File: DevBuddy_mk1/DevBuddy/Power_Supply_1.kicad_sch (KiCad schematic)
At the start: 1 part, among them U5 TPS54331DDAR

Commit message: Changes is hardware - Power
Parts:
- added C10, C11, C18, C19, C20, C9: 4u7, Capacitor_SMD:C_1210_3225Metric, symbol Device:C_Small
- added C12: 6p8, Capacitor_SMD:C_0402_1005Metric, symbol Device:C_Small
- added C13: 3n3, Capacitor_SMD:C_0402_1005Metric, symbol Device:C_Small
- added C14, C21: 8n2, Capacitor_SMD:C_0402_1005Metric, symbol Device:C_Small
- added C15, C22: 100n, Capacitor_SMD:C_0805_2012Metric, symbol Device:C_Small
- added C16, C17: 220u, Capacitor_SMD:CP_Elec_6.3x5.4, symbol Device:C_Polarized_Small
- added C23: 1n, Capacitor_SMD:C_0402_1005Metric, symbol Device:C_Small
- added C24: 10p, Capacitor_SMD:C_0402_1005Metric, symbol Device:C_Small
- added C25, C26, C27: 10u, Capacitor_SMD:C_1210_3225Metric, symbol Device:C_Small
- added C28, C40: 470n, Capacitor_SMD:C_0402_1005Metric, symbol Device:C_Small
- added C29, C39: 2n2, Capacitor_SMD:C_0402_1005Metric, symbol Device:C_Small
- added C30, C31, C37, C38, C41, C42, C46, C47, C48, C49: 22u, Capacitor_SMD:C_0805_2012Metric, symbol Device:C_Small
- added C32, C33, C43, C44: 47u, Capacitor_SMD:C_0805_2012Metric, symbol Device:C_Small
- added C34, C35, C36: 10u, Capacitor_SMD:C_0805_2012Metric, symbol Device:C_Small
- added D1: 550mV 5A, Diode_SMD:D_SMC, symbol Device:D_Small
- added D2: 550mV 2A, Diode_SMD:D_SMC, symbol Device:D_Small
- added FB1, FB2: 0H 1mOhm, symbol Device:FerriteBead_Small
- added L2: 33u, Inductor_SMD:L_Coilcraft_MSS1210-XXX, symbol Device:L_Small
- added L3, L5: 4u7, Inductor_SMD:L_Coilcraft_XAL6060-XXX, symbol Device:L_Small
- added L4: 15u, Inductor_SMD:L_Bourns_SRR1260, symbol Device:L
- added R10: 42k2, Resistor_SMD:R_0402_1005Metric, symbol Device:R_Small
- added R11, R5: 18k7, Resistor_SMD:R_0402_1005Metric, symbol Device:R_Small
- added R12: 28k7, Resistor_SMD:R_0402_1005Metric, symbol Device:R_Small
- added R13, R8: 10k2, Resistor_SMD:R_01005_0402Metric, symbol Device:R_Small
- added R14: 732R, Resistor_SMD:R_01005_0402Metric, symbol Device:R_Small
- added R15, R18: 10k, Resistor_SMD:R_0402_1005Metric, symbol Device:R_Small
- added R16, R19: 15k4, Resistor_SMD:R_0402_1005Metric, symbol Device:R_Small
- added R17, R20: 4k87, Resistor_SMD:R_0402_1005Metric, symbol Device:R_Small
- added R6, R7: 169k, Resistor_SMD:R_0402_1005Metric, symbol Device:R_Small
- added R9: 3k24, Resistor_SMD:R_01005_0402Metric, symbol Device:R_Small
- added U6: TPS54331DDAR, TPS54331DDAR:CONV_TPS54331DDAR, symbol TPS54331DDAR:TPS54331DDAR
- added U7, U8: TPS62913, Package_DFN_QFN:Texas_RPU0010A_VQFN-HR-10_2x2mm_P0.5mm, symbol Regulator_Switching:TPS62913
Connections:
- net at U5.1 (BOOT): now also C15.1
- net VCC: now reaches U5.2 (VIN)
- net VCC: now also C10.1, C11.1, C18.1, C19.1, C20.1, C9.1, R6.1, R7.1, U6.2 (VIN)
- net at U5.3 (EN): now also R5.1, R7.2
- net at U5.4 (SS): now also C14.1
- net at U5.5 (VSENSE): now also R8.1, R9.2
- net at U5.6 (COMP): now also C12.1, R10.1
- net GND: now reaches U5.7 (GND)
- net GND: now also U5.9 (POWERPAD), C10.2, C11.2, C12.2, C13.2, C14.2, C16.2, C17.2, C18.2, C19.2, C20.2, C21.2, C23.2, C24.2, C25.2, C26.2, C27.2, C28.2, C29.2, C30.2, C31.2, C32.2, C33.2, C34.2, C35.2, C36.2, C37.2, C38.2, C39.2, C40.2, C41.2, C42.2, C43.2, C44.2, C46.2, C47.2, C48.2, C49.2, C9.2, D1.2 (A), D2.2 (A), R11.2, R14.1, R17.2, R20.2, R5.2, R9.1, U6.7 (GND), U6.9 (POWERPAD), U7.10 (S-CONF), U7.4 (PGND), U7.7 (PSNS), U8.4 (PGND), U8.7 (PSNS)
- net at U5.8 (PH): now also C15.2, D1.1 (K), L2.1
- new net: C41.1, C42.1, C46.1, C47.1, C48.1, C49.1, FB2.1, L5.2, R18.1, U8.3 (VO)
- new net: C13.1, R10.2
- new net: R18.2, U8.5 (PG)
- new net: L3.1, U7.2 (SW)
- new net: C32.1, C33.1, FB1.1, L3.2, R15.1, U7.3 (VO)
- new net: L5.1, U8.2 (SW)
- new net: C40.1, U8.8 (NR/SS)
- new net: R11.1, R6.2, U6.3 (EN)
- new net: R13.1, R14.2, U6.5 (VSENSE)
- new net: C22.1, U6.1 (BOOT)
- new net: C21.1, U6.4 (SS)
- new net: C24.1, R12.1, U6.6 (COMP)
- new net: C22.2, D2.1 (K), L4.1, U6.8 (PH)
- new net: R15.2, U7.5 (PG)
- new net: C28.1, U7.8 (NR/SS)
- new net: C23.1, R12.2
- new net +12VDC: C25.1, C26.1, C27.1, C29.1, C30.1, C31.1, C37.1, C38.1, C39.1, L4.2, R13.2, U7.1 (EN/SYNC), U7.6 (VIN), U8.1 (EN/SYNC), U8.10 (S-CONF), U8.6 (VIN)
- new net +3V3: C16.1, C17.1, L2.2, R8.2
- new net +3V3_C: C34.1, C35.1, C36.1, FB1.2, R16.1
- new net +5V_C: C43.1, C44.1, FB2.2, R19.1
- new net buck_fb: R16.2, R17.1, R19.2, R20.1, U7.9 (FB), U8.9 (FB)
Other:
- note added: "12V Supply for Low Voltage Clean Channels @2A / 24W"
- note added: "3V3 Logic Power supply @1A / 3.3W (could go up to 6.6W)"
- note added: "3V3 clean Channel Power supply @3A / 9.9W"
- note added: "5V clean Channel Power supply @3A / 15W"
- moved on the sheet: U5

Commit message: Added mux control, fixed adc tlm control, fixed app, added power in PCB
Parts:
- added C45, C50, C53, C54, C64, C67, C68, C70, C72, C75: 22u, Capacitor_SMD:C_0805_2012Metric, symbol Device:C_Small
- added C51, C52, C55: 4u7, Capacitor_SMD:C_1210_3225Metric, symbol Device:C_Small
- added C56, C57: 2n2, Capacitor_SMD:C_0402_1005Metric, symbol Device:C_Small
- added C58, C59: 470n, Capacitor_SMD:C_0402_1005Metric, symbol Device:C_Small
- added C60: 8n2, Capacitor_SMD:C_0402_1005Metric, symbol Device:C_Small
- added C61: 100n, Capacitor_SMD:C_0805_2012Metric, symbol Device:C_Small
- added C62: 1n, Capacitor_SMD:C_0402_1005Metric, symbol Device:C_Small
- added C63, C66, C78, C79: 47u, Capacitor_SMD:C_0805_2012Metric, symbol Device:C_Small
- added C65: 10p, Capacitor_SMD:C_0402_1005Metric, symbol Device:C_Small
- added C69, C71, C73: 10u, Capacitor_SMD:C_0805_2012Metric, symbol Device:C_Small
- added C74, C76, C77: 10u, Capacitor_SMD:C_1210_3225Metric, symbol Device:C_Small
- added D3: 550mV 2A, Diode_SMD:D_SMC, symbol Device:D_Small
- added FB3, FB4: 0H 1mOhm, symbol Device:FerriteBead_Small
- added L6, L7: 4u7, Inductor_SMD:L_Coilcraft_XAL6060-XXX, symbol Device:L_Small
- added L8: 15u, Inductor_SMD:L_Bourns_SRR1260, symbol Device:L
- added R21: 169k, Resistor_SMD:R_0402_1005Metric, symbol Device:R_Small
- added R22: 18k7, Resistor_SMD:R_0402_1005Metric, symbol Device:R_Small
- added R23, R24: 10k, Resistor_SMD:R_0402_1005Metric, symbol Device:R_Small
- added R25: 28k7, Resistor_SMD:R_0402_1005Metric, symbol Device:R_Small
- added R26: 10k2, Resistor_SMD:R_01005_0402Metric, symbol Device:R_Small
- added R27: 732R, Resistor_SMD:R_01005_0402Metric, symbol Device:R_Small
- added R28, R30: 15k4, Resistor_SMD:R_0402_1005Metric, symbol Device:R_Small
- added R29, R31: 4k87, Resistor_SMD:R_0402_1005Metric, symbol Device:R_Small
- added U10, U9: TPS62913, Package_DFN_QFN:Texas_RPU0010A_VQFN-HR-10_2x2mm_P0.5mm, symbol Regulator_Switching:TPS62913
- added U11: TPS54331DDAR, TPS54331DDAR:CONV_TPS54331DDAR, symbol TPS54331DDAR:TPS54331DDAR
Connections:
- net GND: now also C45.2, C50.2, C51.2, C52.2, C53.2, C54.2, C55.2, C56.2, C57.2, C58.2, C59.2, C60.2, C62.2, C63.2, C64.2, C65.2, C66.2, C67.2, C68.2, C69.2, C70.2, C71.2, C72.2, C73.2, C74.2, C75.2, C76.2, C77.2, C78.2, C79.2, D3.2 (A), R22.2, R27.1, R29.2, R31.2, U10.4 (PGND), U10.7 (PSNS), U11.7 (GND), U11.9 (POWERPAD), U9.10 (S-CONF), U9.4 (PGND), U9.7 (PSNS)
- net VCC: now also C51.1, C52.1, C55.1, R21.1, U11.2 (VIN)
- net buck_fb: now also R28.2, R29.1, R30.2, R31.1, U10.9 (FB), U9.9 (FB)
- net +12VDC renamed +12VDC_C
- new net: C61.1, U11.1 (BOOT)
- new net: R21.2, R22.1, U11.3 (EN)
- new net: C60.1, U11.4 (SS)
- new net: R26.1, R27.2, U11.5 (VSENSE)
- new net: C65.1, R25.1, U11.6 (COMP)
- new net: C61.2, D3.1 (K), L8.1, U11.8 (PH)
- new net: C64.1, C67.1, C68.1, C70.1, C72.1, C75.1, FB4.1, L7.2, R24.1, U10.3 (VO)
- new net: L7.1, U10.2 (SW)
- new net: L6.1, U9.2 (SW)
- new net: C63.1, C66.1, FB3.1, L6.2, R23.1, U9.3 (VO)
- new net: R24.2, U10.5 (PG)
- new net: C59.1, U10.8 (NR/SS)
- new net: C62.1, R25.2
- new net: R23.2, U9.5 (PG)
- new net: C58.1, U9.8 (NR/SS)
- new net +12VDC_D: C45.1, C50.1, C53.1, C54.1, C56.1, C57.1, C74.1, C76.1, C77.1, L8.2, R26.2, U10.1 (EN/SYNC), U10.10 (S-CONF), U10.6 (VIN), U9.1 (EN/SYNC), U9.6 (VIN)
- new net +3V3_D: C69.1, C71.1, C73.1, FB3.2, R28.1
- new net +5V_D: C78.1, C79.1, FB4.2, R30.1
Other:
- note added: "12V Supply for Low Voltage Clean Channels @2A / 24W CHANNEL C"
- note added: "12V Supply for Low Voltage Clean Channels @2A / 24W CHANNEL D"
- note added: "3V3 Logic Power supply @1A / 3.3W (could go up to 6.6W) CHANNEL A"
- note added: "3V3 clean Channel Power supply @3A / 9.9W CHANNEL C"
- note added: "3V3 clean Channel Power supply @3A / 9.9W CHANNEL D"
- note added: "5V clean Channel Power supply @3A / 15W CHANNEL C"
- note added: "5V clean Channel Power supply @3A / 15W CHANNEL D"
- note removed: "12V Supply for Low Voltage Clean Channels @2A / 24W"
- note removed: "3V3 Logic Power supply @1A / 3.3W (could go up to 6.6W)"
- note removed: "3V3 clean Channel Power supply @3A / 9.9W"
- note removed: "5V clean Channel Power supply @3A / 15W"

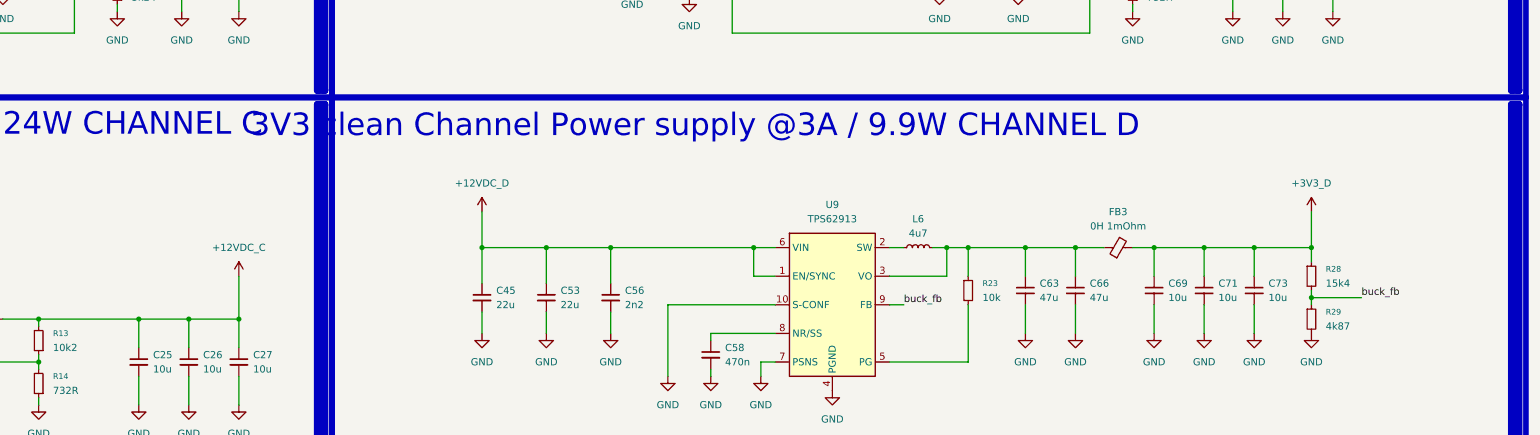
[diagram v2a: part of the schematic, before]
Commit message: Changes in Variable buck - Hardware
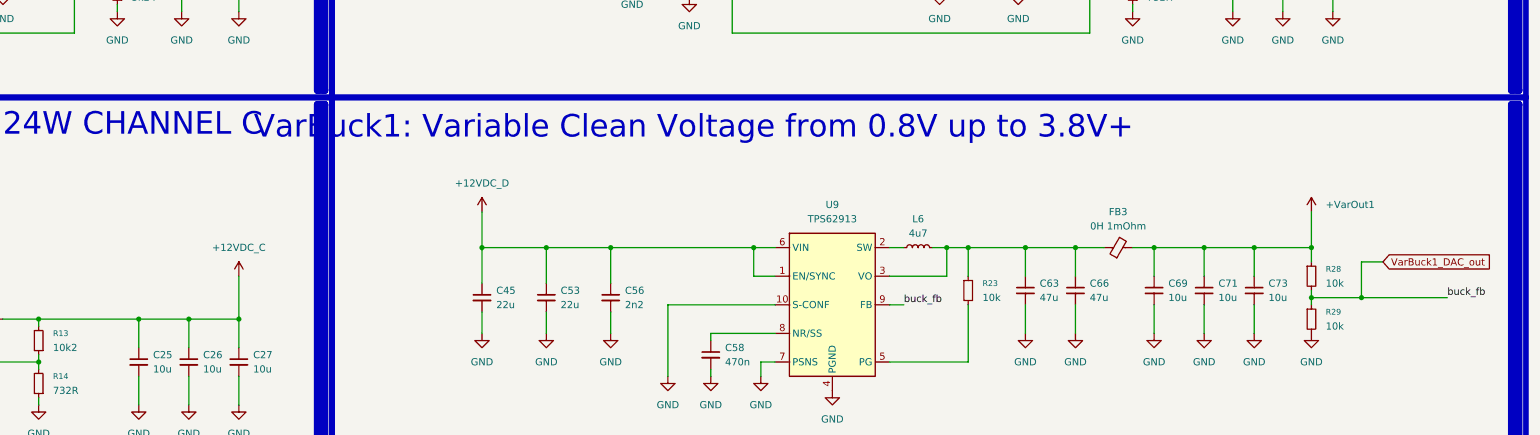
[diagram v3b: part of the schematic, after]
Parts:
- R28: value 15k4 -> 10k
- R29: value 4k87 -> 10k
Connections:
- net +3V3_D renamed +VarOut1
- net buck_fb renamed VarBuck1_DAC_out
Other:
- note added: "VarBuck1: Variable Clean Voltage from 0.8V up to 3.8V+"
- note removed: "3V3 clean Channel Power supply @3A / 9.9W CHANNEL D"
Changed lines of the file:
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@@
 		)
 	)
-	(text "3V3 clean Channel Power supply @3A / 9.9W CHANNEL D\n"
+	(text "VarBuck1: Variable Clean Voltage from 0.8V up to 3.8V+"
 		(exclude_from_sim no)
-		(at 258.826 88.9 0)
+		(at 258.572 89.154 0)
 		(effects
 			(font
@@
 	)
 	(junction
+		(at 377.19 119.38)
+		(diameter 0)
+		(color 0 0 0 0)
+	)
+	(junction
 		(at 44.45 180.34)
 		(diameter 0)
@@
 	(wire
 		(pts
+			(xy 381 113.03) (xy 377.19 113.03)
+		)
+		(stroke
+			(width 0)
+			(type default)
+		)
+	)
+	(wire
+		(pts
 			(xy 378.46 187.96) (xy 378.46 189.23)
 		)
@@
 	(wire
 		(pts
+			(xy 377.19 119.38) (xy 392.43 119.38)
+		)
+		(stroke
+			(width 0)
+			(type default)
+		)
+	)
+	(wire
+		(pts
 			(xy 44.45 250.19) (xy 44.45 256.54)
 		)
@@
 	(wire
 		(pts
+			(xy 377.19 113.03) (xy 377.19 119.38)
+		)
+		(stroke
+			(width 0)
+			(type default)
+		)
+	)
+	(wire
+		(pts
 			(xy 72.39 113.03) (xy 60.96 113.03)
 		)
@@
 	)
 	(label "buck_fb"
-		(at 377.19 119.38 0)
+		(at 392.43 119.38 0)
 		(effects
 			(font
@@
 		)
 	)
+	(global_label "VarBuck1_DAC_out"
+		(shape input)
+		(at 381 113.03 0)
+		(fields_autoplaced yes)
+		(effects
+			(font
+				(size 1.27 1.27)
+			)
+			(justify left)
+		)
+		(property "Intersheetrefs" "${INTERSHEET_REFS}"
+			(at 401.3417 113.03 0)
+			(effects
+				(font
+					(size 1.27 1.27)
+				)
+				(justify left)
+				(hide yes)
+			)
+		)
+	)
 	(symbol
 		(lib_id "power:GND")
@@
 			)
 		)
-		(property "Value" "4k87"
+		(property "Value" "10k"
 			(at 370.84 124.4599 0)
 			(effects
@@
 			)
 		)
-		(property "Value" "15k4"
+		(property "Value" "10k"
 			(at 370.84 116.8399 0)
 			(effects
@@
 			)
 		)
-		(property "Value" "+3V3_D"
-			(at 368.3 99.06 0)
+		(property "Value" "+VarOut1"
+			(at 370.84 102.8699 0)
 			(effects
 				(font
 					(size 1.27 1.27)
 				)
+				(justify left)
 			)
 		)

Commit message: Added variable voltage channels/ PCB
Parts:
- removed C45, C53: 22u, Capacitor_SMD:C_0805_2012Metric, symbol Device:C_Small
- removed C56: 2n2, Capacitor_SMD:C_0402_1005Metric, symbol Device:C_Small
- removed C58: 470n, Capacitor_SMD:C_0402_1005Metric, symbol Device:C_Small
- removed C63, C66: 47u, Capacitor_SMD:C_0805_2012Metric, symbol Device:C_Small
- removed C69, C71, C73: 10u, Capacitor_SMD:C_0805_2012Metric, symbol Device:C_Small
- removed FB3: 0H 1mOhm, symbol Device:FerriteBead_Small
- removed L6: 4u7, Inductor_SMD:L_Coilcraft_XAL6060-XXX, symbol Device:L_Small
- removed R23, R28, R29: 10k, Resistor_SMD:R_0402_1005Metric, symbol Device:R_Small
- removed U9: TPS62913, Package_DFN_QFN:Texas_RPU0010A_VQFN-HR-10_2x2mm_P0.5mm, symbol Regulator_Switching:TPS62913
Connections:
- net VarBuck1_DAC_out renamed buck_fb
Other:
- note removed: "VarBuck1: Variable Clean Voltage from 0.8V up to 3.8V+"

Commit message: Heavy additions to schematic
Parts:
- added R77, R78, R79, R80, R81: 20mOhm, Resistor_SMD:R_1210_3225Metric, symbol Device:R
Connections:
- net +12VDC_C: now also R77.1; no longer C25.1, C26.1, C27.1, L4.2, R13.2
- net +12VDC_D: now also R80.1; no longer C74.1, C76.1, C77.1, L8.2, R26.2
- net +3V3_C: now also R78.1; no longer C34.1, C35.1, C36.1, FB1.2, R16.1
- net +5V_C: now also R79.1; no longer C43.1, C44.1, FB2.2, R19.1
- net +5V_D: now also R81.1; no longer C78.1, C79.1, FB4.2, R30.1
- new net 12V_C_CurSense_Hi: C25.1, C26.1, C27.1, L4.2, R13.2, R77.2
- new net 12V_D_CurSense_Hi: C74.1, C76.1, C77.1, L8.2, R26.2, R80.2
- new net 3V3_C_CurSense_Hi: C34.1, C35.1, C36.1, FB1.2, R16.1, R78.2
- new net 5V_C_CurSense_Hi: C43.1, C44.1, FB2.2, R19.1, R79.2
- new net 5V_D_CurSense_Hi: C78.1, C79.1, FB4.2, R30.1, R81.2

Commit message: PCB, starting the board
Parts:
- FB1: footprint (none) -> Fuse:Fuse_1206_3216Metric; Field5 (none) -> C710518
- FB2, FB4: footprint (none) -> Fuse:Fuse_1206_3216Metric
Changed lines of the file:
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@@
 			)
 		)
-		(property "Footprint" ""
+		(property "Footprint" "Fuse:Fuse_1206_3216Metric"
 			(at 134.62 182.118 90)
 			(effects
@@
 			)
 		)
+		(property "Field5" "C710518"
+			(at 134.62 180.34 90)
+			(effects
+				(font
+					(size 1.27 1.27)
+				)
+				(hide yes)
+			)
+		)
 		(pin "1"
 		)
@@
 			)
 		)
-		(property "Footprint" ""
+		(property "Footprint" "Fuse:Fuse_1206_3216Metric"
 			(at 351.79 182.118 90)
 			(effects
@@
 			)
 		)
-		(property "Footprint" ""
+		(property "Footprint" "Fuse:Fuse_1206_3216Metric"
 			(at 171.45 251.968 90)
 			(effects

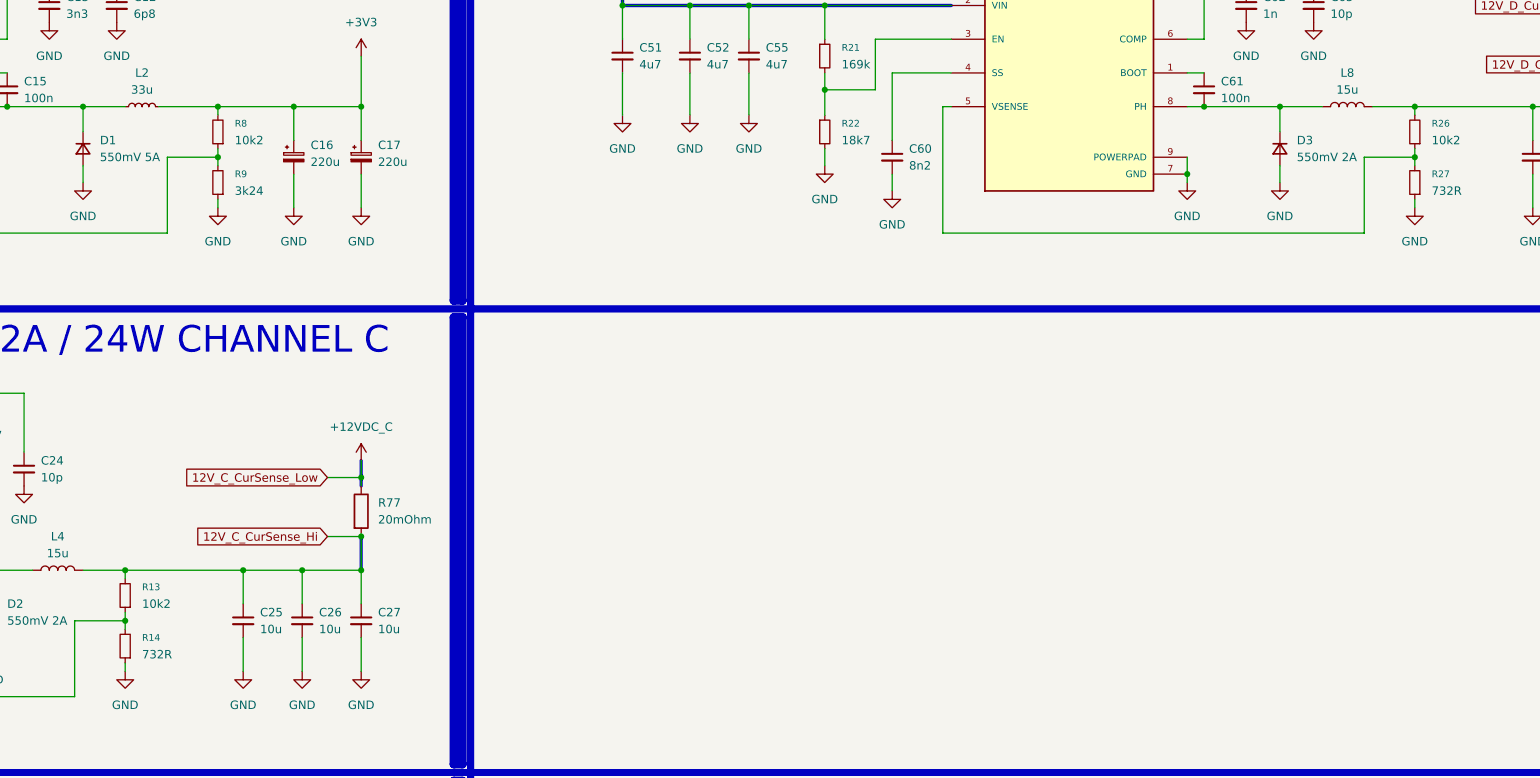
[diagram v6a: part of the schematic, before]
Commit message: PCB, initial routing of submods
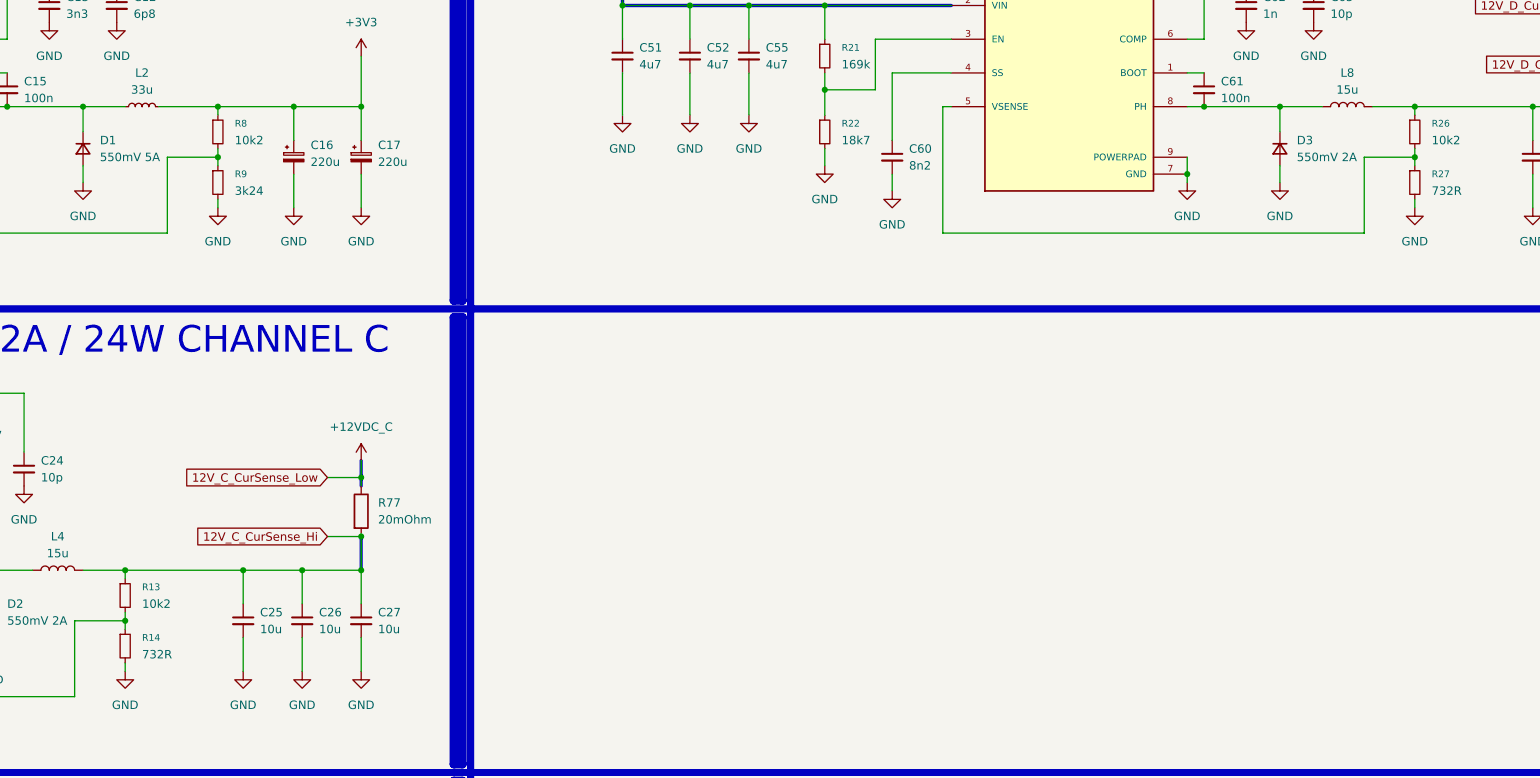
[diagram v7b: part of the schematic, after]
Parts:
- R13, R14, R26, R27, R8, R9: footprint Resistor_SMD:R_01005_0402Metric -> Resistor_SMD:R_0402_1005Metric
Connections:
- net +3V3: now also R8.1; no longer R8.2
- net 12V_C_CurSense_Hi: now also R13.1; no longer R13.2
- net 12V_D_CurSense_Hi: now also R26.1; no longer R26.2
- net GND: now also R14.2, R27.2, R9.2; no longer R14.1, R27.1, R9.1
- new net: R26.2, R27.1, U11.5 (VSENSE)
- new net: R8.2, R9.1, U5.5 (VSENSE)
- new net: R13.2, R14.1, U6.5 (VSENSE)

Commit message: PCB, Power routing nearly complete.
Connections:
- net buck_fb: no longer R19.2, R20.1, R30.2, R31.1, U10.9 (FB), U8.9 (FB)
- new net buck_fb1: R19.2, R20.1, U8.9 (FB)
- new net buck_fb2: R30.2, R31.1, U10.9 (FB)
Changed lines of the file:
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@@
 		)
 	)
-	(label "buck_fb"
+	(label "buck_fb2"
 		(at 387.35 189.23 0)
 		(effects
@@
 		)
 	)
-	(label "buck_fb"
+	(label "buck_fb1"
 		(at 207.01 259.08 0)
 		(effects
@@
 		)
 	)
-	(label "buck_fb"
+	(label "buck_fb2"
 		(at 276.86 190.5 0)
 		(effects
@@
 		)
 	)
-	(label "buck_fb"
+	(label "buck_fb1"
 		(at 96.52 260.35 0)
 		(effects
